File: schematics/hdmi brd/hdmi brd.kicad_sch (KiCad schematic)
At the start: 25 parts, among them J1 Conn_02x32_Odd_Even, J2 685119134923

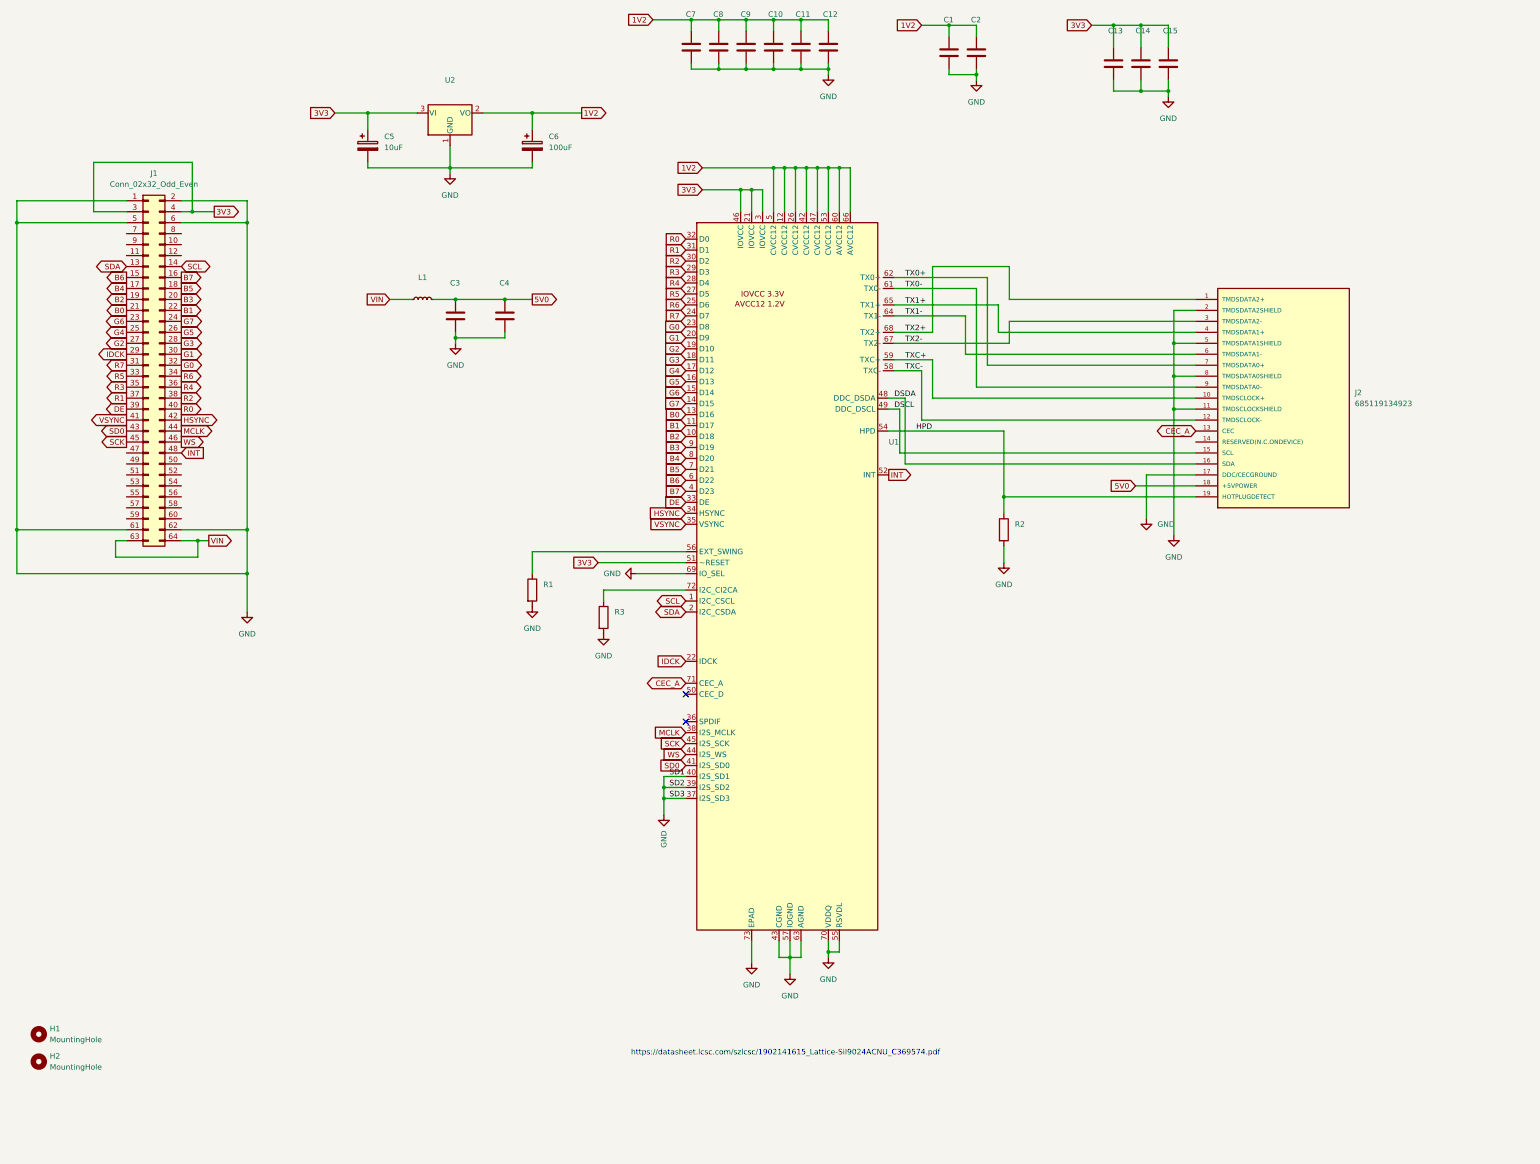
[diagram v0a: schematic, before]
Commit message: Rv32: Rev 2 of HDMI board. Ordered from JLCPCB.
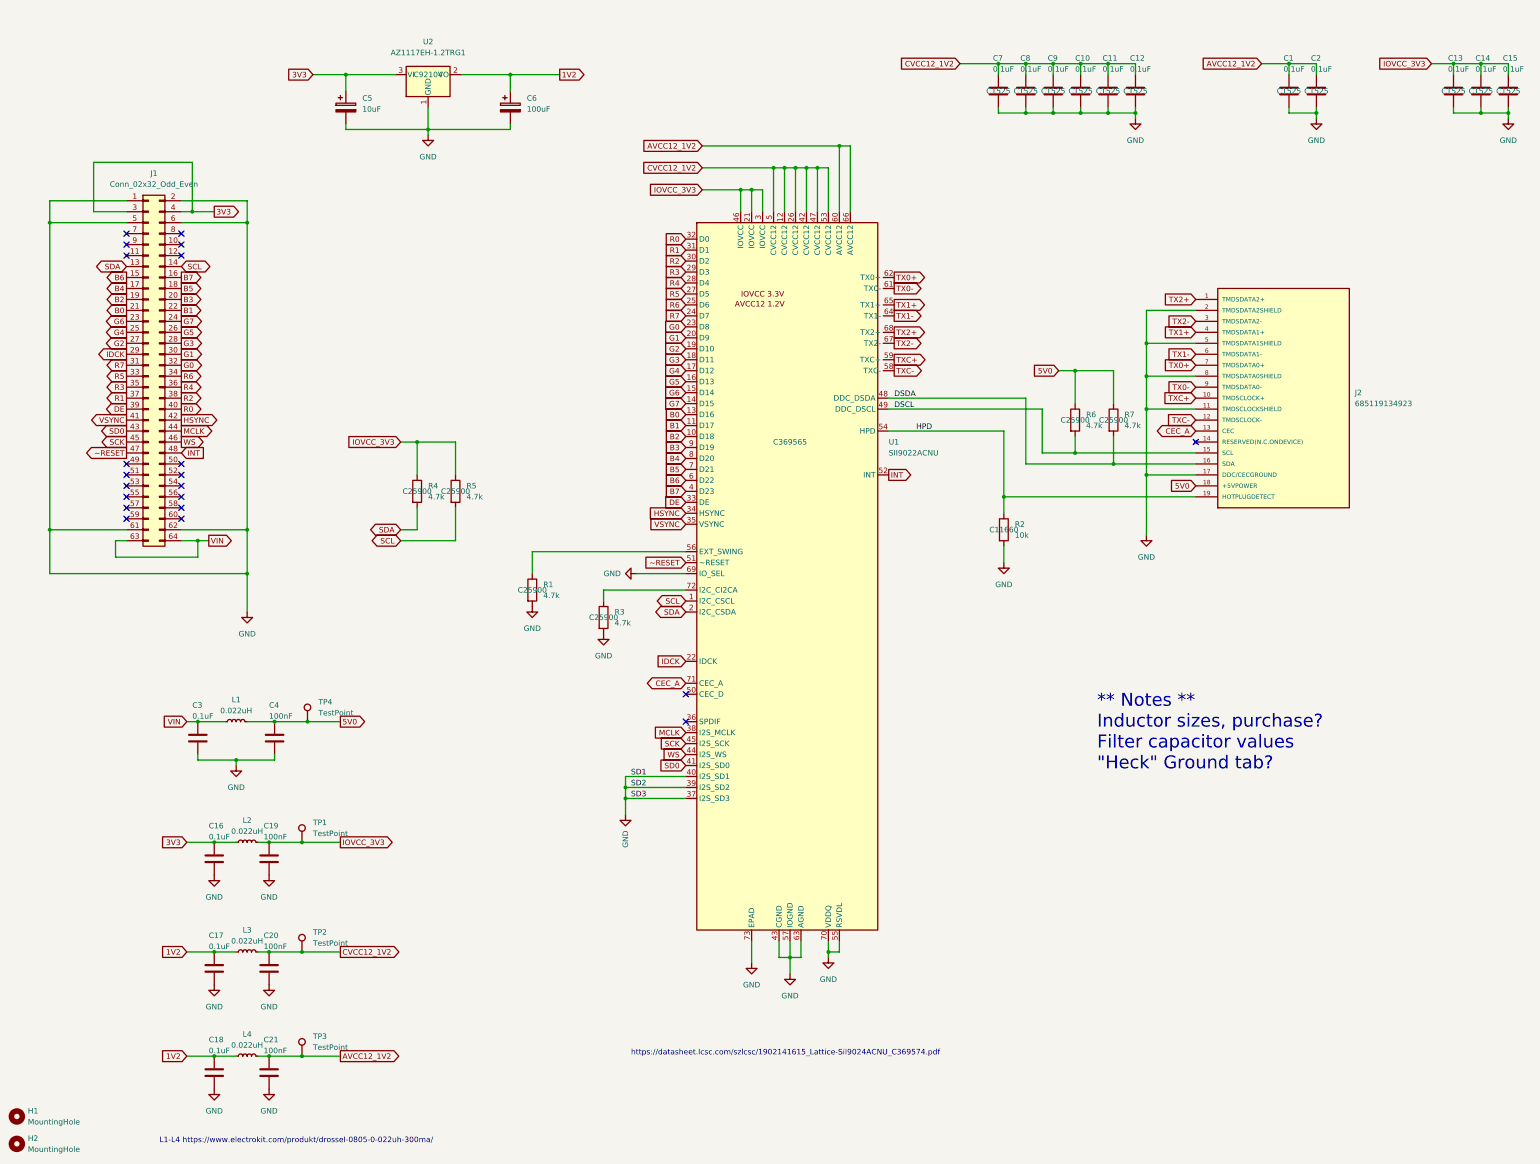
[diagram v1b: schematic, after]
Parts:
- added C16, C17, C18: 0.1uF, Capacitor_SMD:C_0805_2012Metric_Pad1.18x1.45mm_HandSolder, symbol Device:C
- added C19, C20, C21: 100nF, Capacitor_SMD:C_0805_2012Metric_Pad1.18x1.45mm_HandSolder, symbol Device:C
- added L2, L3, L4: 0.022uH, Inductor_SMD:L_0805_2012Metric_Pad1.15x1.40mm_HandSolder, symbol Device:L_Small
- added R4, R5, R6, R7: 4.7k, Resistor_SMD:R_0402_1005Metric, symbol Device:R
- added TP1, TP2, TP3, TP4: TestPoint, TestPoint:TestPoint_Pad_D1.0mm, symbol Connector:TestPoint
- C1, C10, C11, C12, C13, C14, C15, C2, C7, C8, C9: value (none) -> 0.1uF; footprint (none) -> Capacitor_SMD:C_0402_1005Metric
- C3: value (none) -> 0.1uF; footprint (none) -> Capacitor_SMD:C_0805_2012Metric_Pad1.18x1.45mm_HandSolder
- C4: value (none) -> 100nF; footprint (none) -> Capacitor_SMD:C_0805_2012Metric_Pad1.18x1.45mm_HandSolder
- J2: LCSC (none) -> C720616
- L1: value (none) -> 0.022uH; footprint (none) -> Inductor_SMD:L_0805_2012Metric_Pad1.05x1.20mm_HandSolder
- R1, R3: value (none) -> 4.7k; footprint (none) -> Resistor_SMD:R_0402_1005Metric
- R2: value (none) -> 10k; footprint (none) -> Resistor_SMD:R_0402_1005Metric; LCSC (none) -> C11660
- U1: value (none) -> SII9022ACNU; footprint (none) -> Package_DFN_QFN:QFN-72-1EP_10x10mm_P0.5mm_EP6x6mm
- U2: value (none) -> AZ1117EH-1.2TRG1; footprint (none) -> Package_TO_SOT_SMD:SOT-223-3_TabPin2
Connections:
- net 1V2: now also C17.1, C18.1, L3.1, L4.1; no longer C1.1, C10.1, C11.1, C12.1, C2.1, C7.1, C8.1, C9.1, U1.12 (CVCC12), U1.26 (CVCC12), U1.42 (CVCC12), U1.47 (CVCC12), U1.5 (CVCC12), U1.53 (CVCC12), U1.60 (AVCC12), U1.66 (AVCC12)
- net 3V3: now also C16.1, L2.1; no longer C13.1, C14.1, C15.1, U1.21 (IOVCC), U1.3 (IOVCC), U1.46 (IOVCC), U1.51 (~RESET)
- net 5V0: now also R6.1, R7.1, TP4.1; no longer C3.1
- net DSCL: now also R6.2
- net DSDA: now also R7.2
- net GND: now also C16.2, C17.2, C18.2, C19.2, C20.2, C21.2
- net SCL: now also R5.2
- net SDA: now also R4.2
- net VIN: now also C3.1
- net ~RESET: now reaches J1.47 (Pin_47)
- net ~RESET: now also U1.51 (~RESET)
- new net AVCC12_1V2: C1.1, C2.1, C21.1, L4.2, TP3.1, U1.60 (AVCC12), U1.66 (AVCC12)
- new net CVCC12_1V2: C10.1, C11.1, C12.1, C20.1, C7.1, C8.1, C9.1, L3.2, TP2.1, U1.12 (CVCC12), U1.26 (CVCC12), U1.42 (CVCC12), U1.47 (CVCC12), U1.5 (CVCC12), U1.53 (CVCC12)
- new net IOVCC_3V3: C13.1, C14.1, C15.1, C19.1, L2.2, R4.1, R5.1, TP1.1, U1.21 (IOVCC), U1.3 (IOVCC), U1.46 (IOVCC)
- no-connect marks 2 -> 21
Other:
- note added: "** Notes ** Inductor sizes, purchase? Filter capacitor values "Heck" Ground tab?"
- note added: "L1-L4 https://www.electrokit.com/produkt/drossel-0805-0-022uh-300ma/"
- moved on the sheet: C1, C10, C11, C12, C13, C14, C15, C2, C3, C4, C5, C6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
